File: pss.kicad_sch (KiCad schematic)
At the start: 0 parts

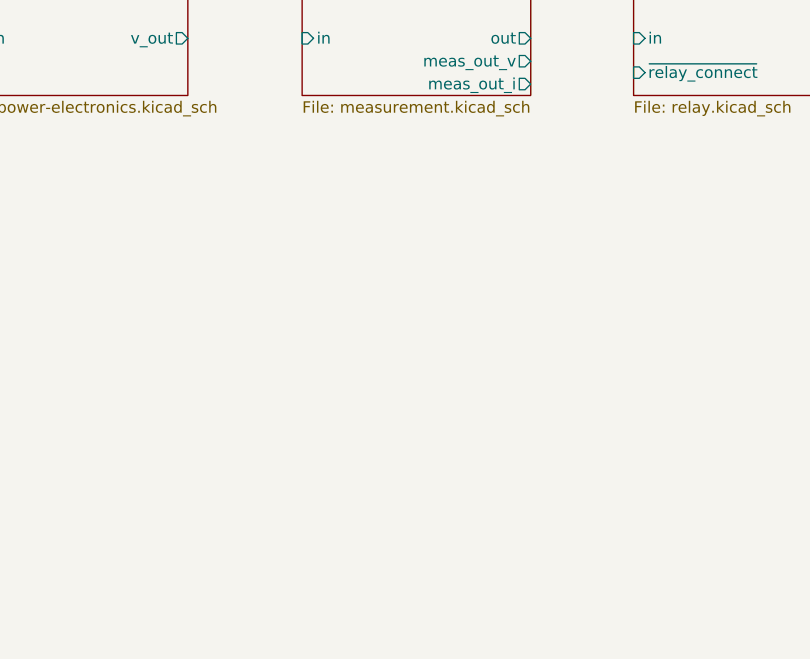
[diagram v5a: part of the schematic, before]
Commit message: add adc hierarchical sub circuit
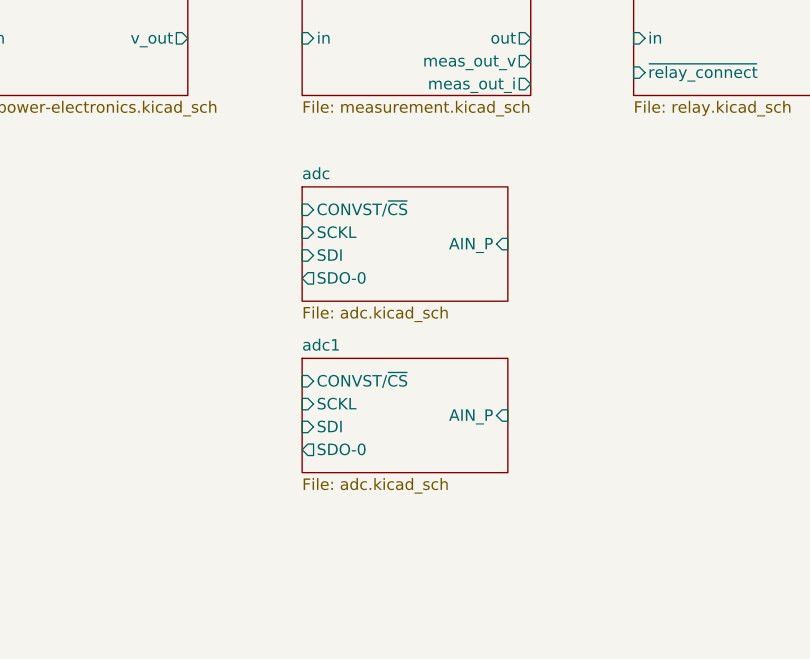
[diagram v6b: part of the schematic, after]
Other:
- added sheet adc (adc.kicad_sch)
- added sheet adc1 (adc.kicad_sch)
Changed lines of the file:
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@@
+	)
+	(sheet
+		(at 194.31 120.65)
+		(size 22.86 12.7)
+		(fields_autoplaced yes)
+		(stroke
+			(width 0.1524)
+			(type solid)
+		)
+		(fill
+			(color 0 0 0 0.0000)
+		)
+		(property "Sheetname" "adc"
+			(at 194.31 119.9384 0)
+			(effects
+				(font
+					(size 1.27 1.27)
+				)
+				(justify left bottom)
+			)
+		)
+		(property "Sheetfile" "adc.kicad_sch"
+			(at 194.31 133.9346 0)
+			(effects
+				(font
+					(size 1.27 1.27)
+				)
+				(justify left top)
+			)
+		)
+		(pin "AIN_P" input
+			(at 217.17 127 0)
+			(effects
+				(font
+					(size 1.27 1.27)
+				)
+				(justify right)
+			)
+		)
+		(pin "SDO-0" output
+			(at 194.31 130.81 180)
+			(effects
+				(font
+					(size 1.27 1.27)
+				)
+				(justify left)
+			)
+		)
+		(pin "SDI" input
+			(at 194.31 128.27 180)
+			(effects
+				(font
+					(size 1.27 1.27)
+				)
+				(justify left)
+			)
+		)
+		(pin "SCKL" input
+			(at 194.31 125.73 180)
+			(effects
+				(font
+					(size 1.27 1.27)
+				)
+				(justify left)
+			)
+		)
+		(pin "CONVST{slash}~{CS}" input
+			(at 194.31 123.19 180)
+			(effects
+				(font
+					(size 1.27 1.27)
+				)
+				(justify left)
+			)
+		)
+		(instances
+			(project "pss"
+				(path "/3c438cf7-9350-4e9f-8115-1deba8984176"
+					(page "16")
+				)
+			)
+		)
 	)
 	(sheet
@@
 				)
 			)
+		)
+	)
+	(sheet
+		(at 194.31 139.7)
+		(size 22.86 12.7)
+		(fields_autoplaced yes)
+		(stroke
+			(width 0.1524)
+			(type solid)
+		)
+		(fill
+			(color 0 0 0 0.0000)
+		)
+		(property "Sheetname" "adc1"
+			(at 194.31 138.9884 0)
+			(effects
+				(font
+					(size 1.27 1.27)
+				)
+				(justify left bottom)
+			)
+		)
+		(property "Sheetfile" "adc.kicad_sch"
+			(at 194.31 152.9846 0)
+			(effects
+				(font
+					(size 1.27 1.27)
+				)
+				(justify left top)
+			)
+		)
+		(pin "AIN_P" input
+			(at 217.17 146.05 0)
+			(effects
+				(font
+					(size 1.27 1.27)
+				)
+				(justify right)
+			)
+		)
+		(pin "SDO-0" output
+			(at 194.31 149.86 180)
+			(effects
+				(font
+					(size 1.27 1.27)
+				)
+				(justify left)
+			)
+		)
+		(pin "SDI" input
+			(at 194.31 147.32 180)
+			(effects
+				(font
+					(size 1.27 1.27)
+				)
+				(justify left)
+			)
+		)
+		(pin "SCKL" input
+			(at 194.31 144.78 180)
+			(effects
+				(font
+					(size 1.27 1.27)
+				)
+				(justify left)
+			)
+		)
+		(pin "CONVST{slash}~{CS}" input
+			(at 194.31 142.24 180)
+			(effects
+				(font
+					(size 1.27 1.27)
+				)
+				(justify left)
+			)
+		)
+		(instances
+			(project "pss"
+				(path "/3c438cf7-9350-4e9f-8115-1deba8984176"
+					(page "18")
+				)
+			)

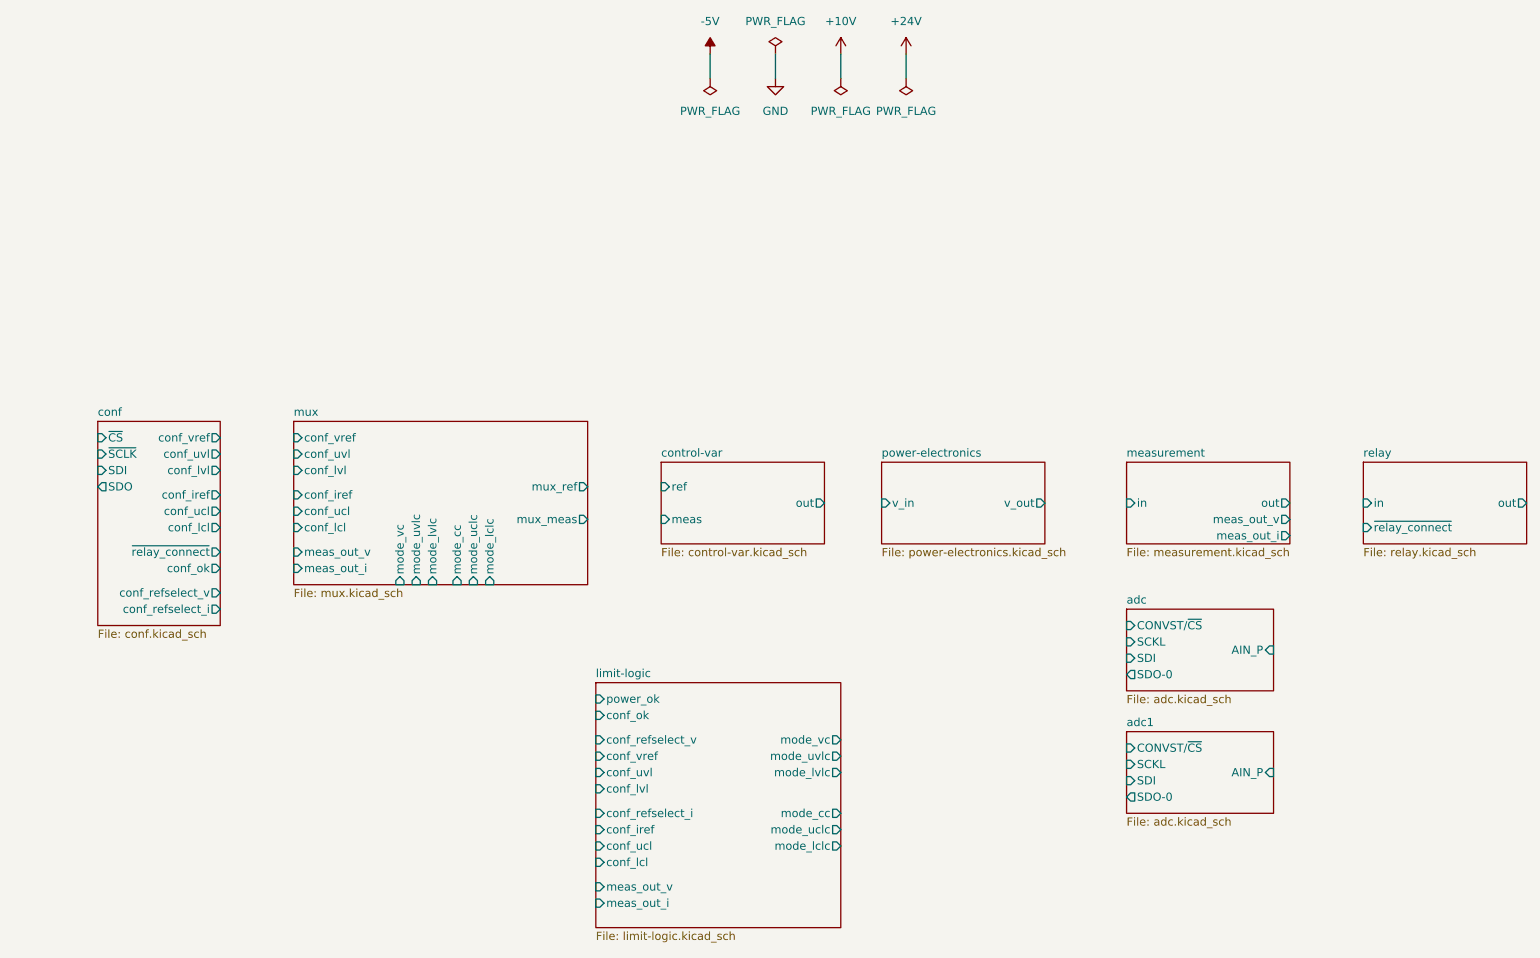
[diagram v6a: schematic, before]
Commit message: add digital-interface component
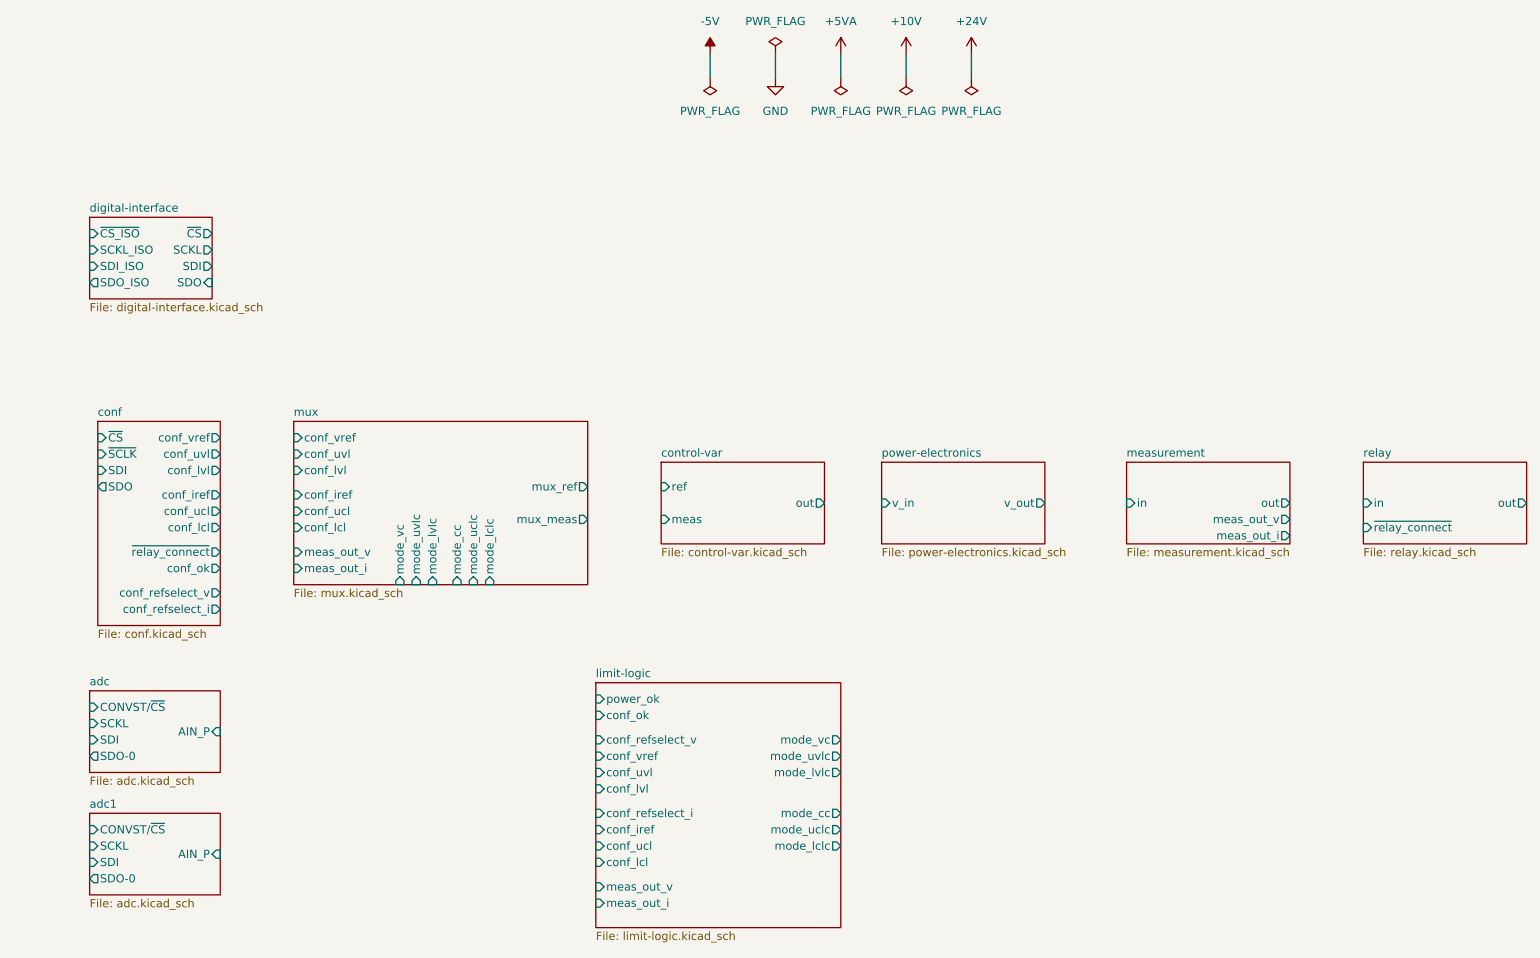
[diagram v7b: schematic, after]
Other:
- added sheet digital-interface (digital-interface.kicad_sch)
